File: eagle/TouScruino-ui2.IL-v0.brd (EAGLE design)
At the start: 53.3 x 50.8 mm, 3 parts, among them U1 TFT_20

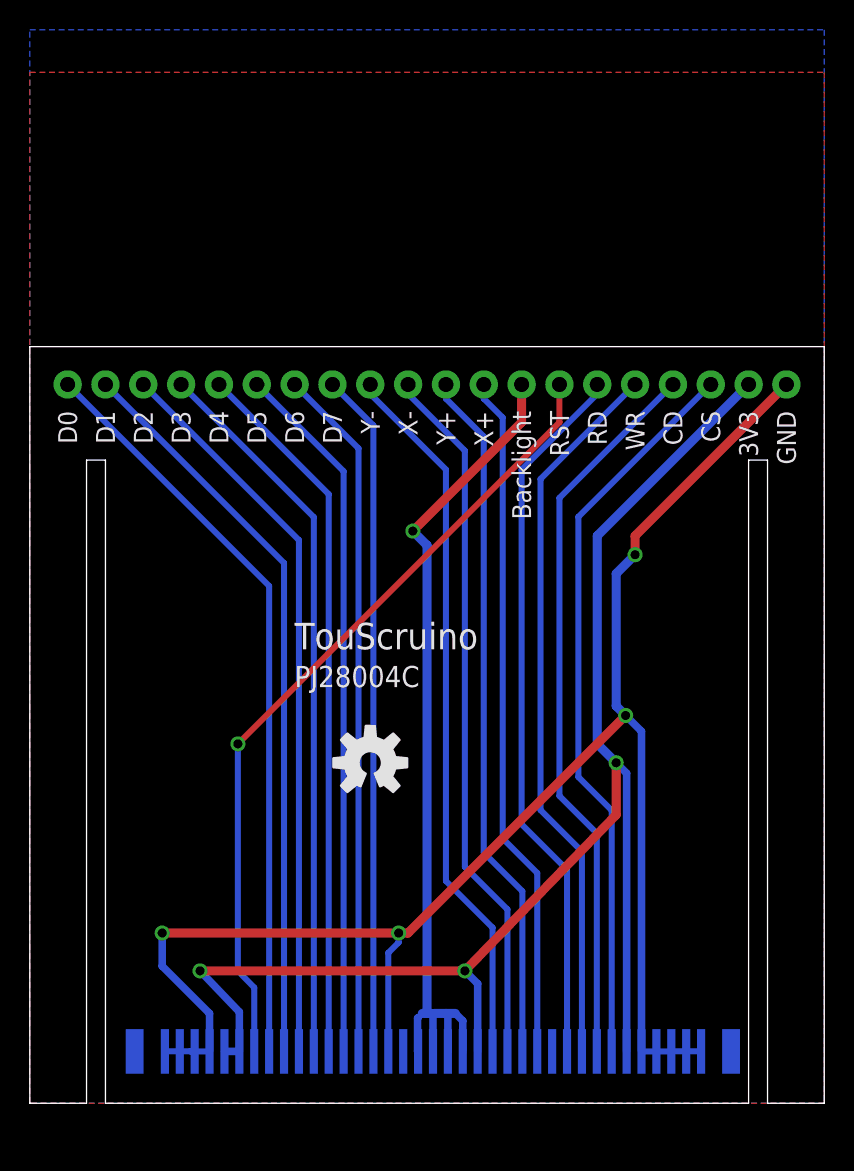
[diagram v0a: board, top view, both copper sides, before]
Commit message: 
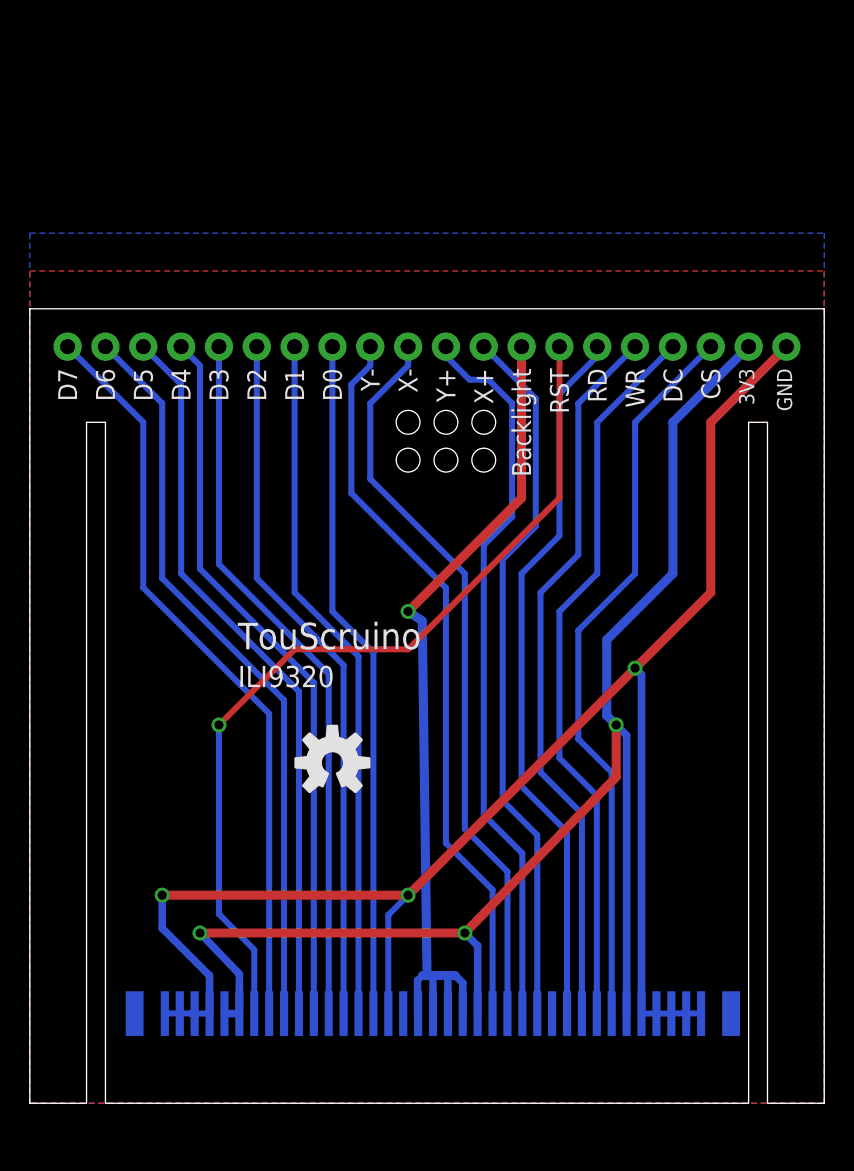
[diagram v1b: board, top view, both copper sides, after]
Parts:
- U1: device wibauxl:1X20 -> wibauxl:TFT_20
- moved U$2 2.54 mm to (52.1, -20.5)
- moved U$3 2.54 mm to (20.3, 22.9)
- moved U1 2.54 mm to (2.54, 50.8), flipped to the bottom
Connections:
- net N$1 renamed VCC
- net N$10 renamed D31
- net N$11 renamed D22
- net N$12 renamed D23
- net N$13 renamed D21
- net N$14 renamed D16
- net N$15 renamed D17
- net N$16 renamed D18
- net N$17 renamed D11
- net N$18 renamed D12
- net N$19 renamed D13
- net N$2 renamed BL
- net N$3 renamed D14
- net N$4 renamed D15
- net N$5 renamed Y-
- net N$6 renamed Y+
- net N$7 renamed X-
- net N$8 renamed X+
- net N$9 renamed RES
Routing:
- net RES: track 54.2 -> 59.7 mm
- net Y+: track 46.9 -> 49.2 mm
- net X-: track 47.5 -> 49.6 mm
- net X+: track 46.3 -> 48.1 mm
- net Y-: track 48.2 -> 49.2 mm
- net VCC: track 98.9 -> 98.4 mm
- net GND: track 112.3 -> 112.5 mm, vias 4 -> 3
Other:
- board size 53.3 x 50.8 mm -> 53.3 x 53.3 mm
- board text added: "DC"
- board text added: "ILI9320"
- board text removed: "CD"
- board text removed: "PJ28004C"

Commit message: 
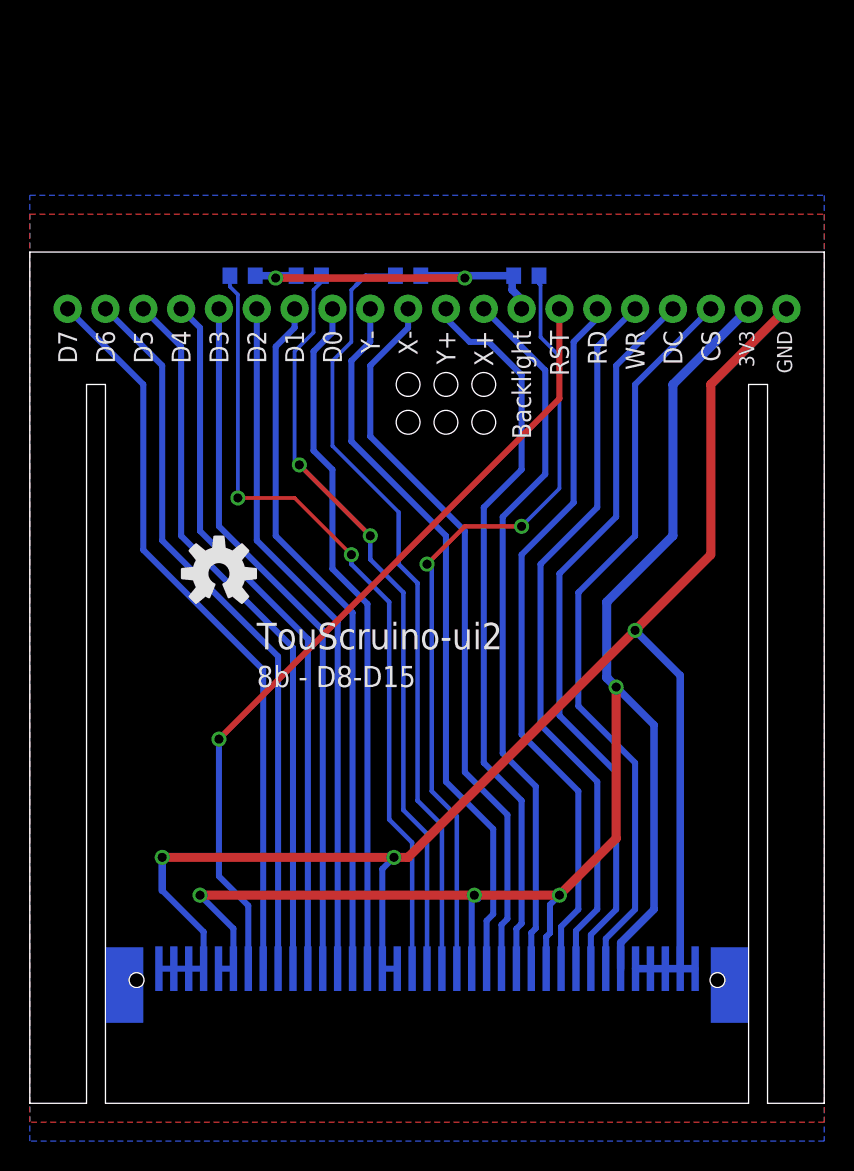
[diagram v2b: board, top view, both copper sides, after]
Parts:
- removed U$2: TFT_2.8_37, wibauxl:TFT_2.8_37
- removed U1: TFT_20, wibauxl:TFT_20
- added CN1: (no value), adafruit:ILI9325_28INCH_TS
- added JP1: TFT_20, wibauxl:TFT_20
- added R1, R2, R3, R4: 10, resistor:R0603
- moved U$3 14.8 mm to (12.7, 35.6)
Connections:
- removed net D11: U$2.28, U1.3
- removed net D12: U$2.29, U1.2
- removed net D13: U$2.30, U1.1
- removed net D14: U$2.23, U1.8
- removed net D15: U$2.24, U1.7
- removed net D16: U$2.25, U1.6
- removed net D17: U$2.26, U1.5
- removed net D18: U$2.27, U1.4
- removed net D21: U$2.7, U1.18
- removed net D22: U$2.9, U1.16
- removed net D23: U$2.10, U1.15
- removed net D31: U$2.8, U1.17
- removed net RES: U$2.31, U1.14
- new net CS: CN1.7, JP1.18
- new net D/C: CN1.8, JP1.17
- new net D0: CN1.23, JP1.8
- new net D1: CN1.24, JP1.7
- new net D2: CN1.25, JP1.6
- new net D3: CN1.26, JP1.5
- new net D4: CN1.27, JP1.4
- new net D5: CN1.28, JP1.3
- new net D6: CN1.29, JP1.2
- new net D7: CN1.30, JP1.1
- new net L1: CN1.17, R1.1
- new net L2: CN1.18, R2.1
- new net L3: CN1.19, R3.1
- new net L4: CN1.20, R4.1
- new net RD: CN1.10, JP1.15
- new net RST: CN1.31, JP1.14
- new net WR: CN1.9, JP1.16
- net BL: now also JP1.13, R1.2, R2.2, R3.2, R4.2; no longer U$2.17, U$2.18, U$2.19, U$2.20, U1.13
- net GND: now also CN1.1, CN1.2, CN1.21, CN1.22, CN1.3, CN1.34, CN1.35, CN1.36, CN1.37, CN1.4, CN1.5, JP1.20; no longer U$2.1, U$2.2, U$2.22, U$2.3, U$2.34, U$2.35, U$2.36, U$2.37, U$2.4, U$2.5, U1.20
- net VCC: now also CN1.11, CN1.16, CN1.32, CN1.33, CN1.6, JP1.19; no longer U$2.16, U$2.32, U$2.33, U$2.6, U1.19
- net X+: now also CN1.12, JP1.12; no longer U$2.12, U1.12
- net X-: now also CN1.14, JP1.10; no longer U$2.14, U1.10
- net Y+: now also CN1.13, JP1.11; no longer U$2.13, U1.11
- net Y-: now also CN1.15, JP1.9; no longer U$2.15, U1.9
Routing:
- net RES: track 59.7 -> 0.00 mm, vias 1 -> 0
- net RST: track 0.00 -> 54.6 mm, vias 0 -> 1
- net L1: track 0.00 -> 53.8 mm, vias 0 -> 2
- net L4: track 0.00 -> 53.8 mm, vias 0 -> 2
- net L2: track 0.00 -> 53.1 mm
- net L3: track 0.00 -> 51.3 mm, vias 0 -> 2
- net D13: track 50.4 -> 0.00 mm
- net CS: track 0.00 -> 50.4 mm
- net D12: track 49.7 -> 0.00 mm
- net D7: track 0.00 -> 49.7 mm
- net D/C: track 0.00 -> 49.7 mm
- net D21: track 49.4 -> 0.00 mm
- net D11: track 49.1 -> 0.00 mm
- net D6: track 0.00 -> 49.1 mm
- net WR: track 0.00 -> 49.1 mm
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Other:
- board size 53.3 x 53.3 mm -> 53.3 x 57.1 mm
- board text added: "8b - D8-D15"
- board text added: "TouScruino-ui2"
- board text removed: "ILI9320"
- board text removed: "TouScruino"
